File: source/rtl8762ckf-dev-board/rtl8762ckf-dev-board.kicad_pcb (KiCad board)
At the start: 2 copper layers, 87.6 x 17.8 mm, 123 parts, among them J1 u.FL, J2 USB_C_Receptacle_USB2.0, J3 Conn_02x05_Odd_Even, J4 Conn_02x05_Odd_Even, J5 Conn_01x18, J6 boot, J7 Conn_01x03, J9 Conn_01x13, Q1 BC807DS,115, Q2 AO3401A, U2 USBLC6-2SC6, U3 ME6211C33M5G-N, U4 STM32F103C8Tx, U5 RTL8762CKF, Y1 40MHz, Y2 8MHz

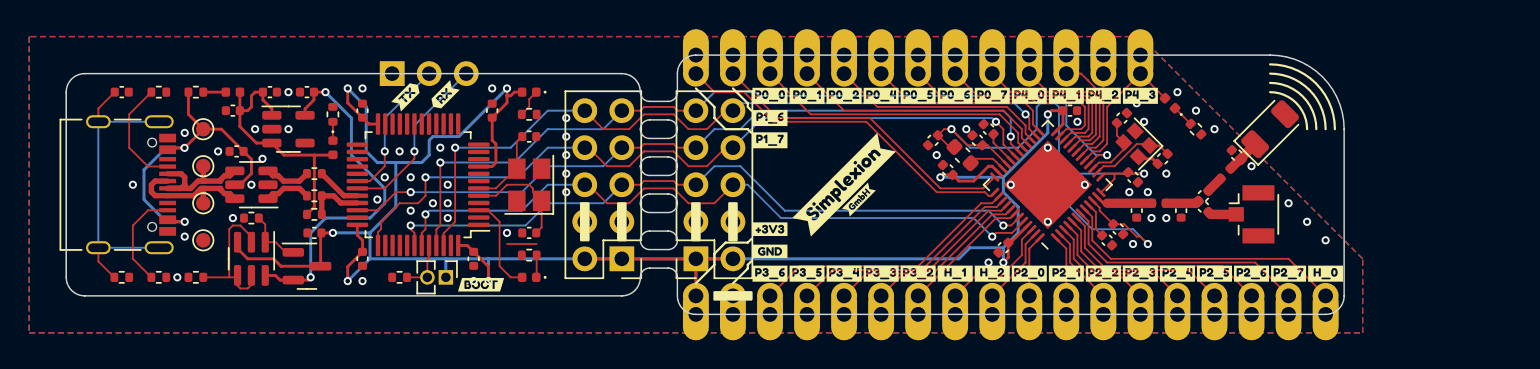
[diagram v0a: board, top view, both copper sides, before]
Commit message: implemented pico probe
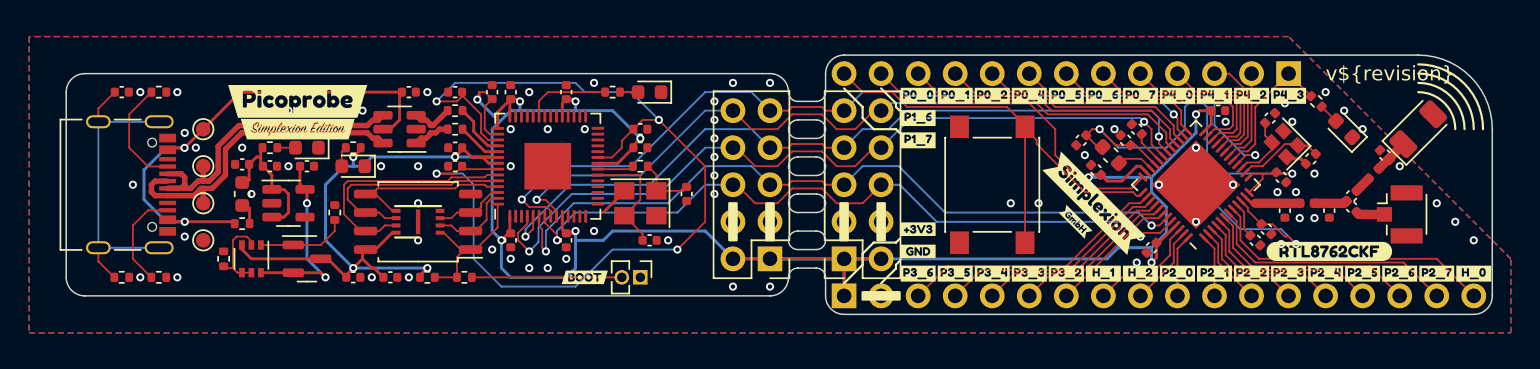
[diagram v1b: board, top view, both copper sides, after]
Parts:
- removed the C22 at (158.8, 130.3)
- removed the J7 at (149.4, 119.4)
- removed J9: Conn_01x13, Connector_Castellated:Castellated_1x13_P2.54mm
- removed the R6 at (149.9, 133.3)
- removed the R7 at (144.0, 127.8)
- removed the R8 at (144.0, 126.2)
- removed the R9 at (144.0, 129.0)
- removed U4: STM32F103C8Tx, Package_QFP:LQFP-48_7x7mm_P0.5mm
- removed kibuzzard-641D9E09: G***, kibuzzard-641D9E09
- removed kibuzzard-641D9E28: G***, kibuzzard-641D9E28
- added C28: 100n, Capacitor_SMD:C_0402_1005Metric, F.Cu at (153.7, 125.7)
- added C29: 100n, Capacitor_SMD:C_0402_1005Metric, F.Cu at (153.7, 124.5)
- added C30: 100n, Capacitor_SMD:C_0402_1005Metric, F.Cu at (161.3, 130.8)
- added C31: 1u, Capacitor_SMD:C_0402_1005Metric, F.Cu at (156.2, 120.7)
- added C32: 100n, Capacitor_SMD:C_0402_1005Metric, F.Cu at (157.5, 130.8)
- added C33: 100n, Capacitor_SMD:C_0402_1005Metric, F.Cu at (157.5, 120.7)
- added C34: 100n, Capacitor_SMD:C_0402_1005Metric, F.Cu at (161.3, 120.7)
- added C35: 100n, Capacitor_SMD:C_0402_1005Metric, F.Cu at (166.4, 124.5)
- added J4: Conn_01x13, Connector_PinHeader_2.54mm:PinHeader_1x13_P2.54mm_Vertical, B.Cu at (210.8, 119.4)
- added NT1: NetTie_2, NetTie_Project:NetTie-2_SMD_Pad0.127mm, F.Cu at (153.7, 121.3)
- added NT2: NetTie_2, NetTie_Project:NetTie-2_SMD_Pad0.127mm, F.Cu at (155.4, 120.7)
- added R10: 1k, Resistor_SMD:R_0402_1005Metric, F.Cu at (154.3, 133.3)
- added R11: 10k, Resistor_SMD:R_0402_1005Metric, F.Cu at (151.8, 133.3)
- added R12: 22, Resistor_SMD:R_0402_1005Metric, F.Cu at (153.7, 123.2)
- added R13: 22, Resistor_SMD:R_0402_1005Metric, F.Cu at (153.7, 121.9)
- added R14: 1k, Resistor_SMD:R_0402_1005Metric, F.Cu at (166.4, 125.7)
- added SW1: SW_Push, Button_Switch_SMD:SW_Push_1P1T_NO_6x6mm_H9.5mm, F.Cu at (190.5, 127.0)
- added U5: W25Q16JV, Package_USON:USON-8_3.0x2.0mm_P0.5mm, F.Cu at (151.1, 129.5)
- added U6: RP2040, Package_DFN_QFN:QFN-56-1EP_7x7mm_P0.4mm_EP3.2x3.2mm, F.Cu at (160.0, 125.7)
- added U7: W25Q128JVS, Package_SO:SOIC-8_5.23x5.23mm_P1.27mm, F.Cu at (151.1, 129.5)
- added kibuzzard-642D5EF2: G***, kibuzzard-642D5EF2, F.Cu at (142.9, 121.3)
- added kibuzzard-642D5F02: G***, kibuzzard-642D5F02, F.Cu at (142.9, 123.2)
- added kibuzzard-642D619C: G***, kibuzzard-642D619C, F.Cu at (213.6, 131.6)
- AE1: value Antenna_Chip -> 2.4GHz
- C12: renamed from C9; value DNP -> C
- C23: value DNP -> 100n
- C24, C25: value 100n -> 33p
- C27: value 100n -> 1u
- C5: renamed from C2; value 3.8p -> 3.9p
- C6: renamed from C3; value DNP -> 22p
- C8: renamed from C5; value 9.2p -> 9.1p
- C9: renamed from C6; value DNP -> C
- D1: renamed from D3; footprint LED_SMD:LED_0402_1005Metric -> LED_SMD:LED_0603_1608Metric
- D2: footprint LED_SMD:LED_0402_1005Metric -> LED_SMD:LED_0603_1608Metric
- D3: renamed from D4; footprint LED_SMD:LED_0402_1005Metric -> LED_SMD:LED_0603_1608Metric
- D4: renamed from D1; footprint LED_SMD:LED_0402_1005Metric -> LED_SMD:LED_0603_1608Metric
- FB1: footprint Inductor_SMD:L_0402_1005Metric -> Inductor_SMD:L_0603_1608Metric
- J5: footprint Connector_Castellated:Castellated_1x18_P2.54mm -> Connector_PinHeader_2.54mm:PinHeader_1x18_P2.54mm_Vertical; moved to B.Cu
- Q1: footprint Package_SO:SC-74-6_1.5x2.9mm_P0.95mm -> Package_TO_SOT_SMD:SOT-363_SC-70-6
- R5: renamed from R1; value 1M -> 10k
- Y2: value 8MHz -> 12M
- moved C25 22.9 mm to (169.5, 127.6)
- moved C24 19.7 mm to (167.0, 130.8), turned to 0 degrees
- moved kibuzzard-641A4D28 17.2 mm to (197.5, 128.3), turned to -45 degrees
- moved D2 15.1 mm to (167.0, 120.7)
- moved kibuzzard-641CD305 14.9 mm to (196.2, 129.5), turned to -45 degrees
- moved C23 13.6 mm to (149.2, 133.3)
- moved J1 13.3 mm to (166.4, 133.3)
- moved D3 13.1 mm to (146.7, 125.7)
- moved R2 12.6 mm to (164.5, 120.7), turned to 180 degrees
- moved C21 12.5 mm to (150.5, 120.7), turned to 180 degrees
- moved R3 12.3 mm to (146.7, 124.5), turned to 0 degrees
- moved D4 12.1 mm to (214.6, 123.2)
- moved C27 11.5 mm to (153.7, 120.7), turned to 180 degrees
- moved U3 10.9 mm to (149.9, 123.2)
- moved C26 10.2 mm to (166.4, 123.2), turned to 0 degrees
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- renumbered C20 to C1, C7 to C10, C8 to C11, C10 to C13, C11 to C14, C12 to C15, C13 to C16, C14 to C17, C15 to C18, C16 to C19, C28 to C2, C17 to C20, C18 to C21, C19 to C22, C21 to C3, C1 to C4, C4 to C7, J6 to J1, J3 to J2, J4 to J3, J1 to J6, J2 to J7, R12 to R1, R11 to R2, R13 to R3, R10 to R4, R2 to R6, R3 to R7, R4 to R8, R5 to R9, U3 to U1, U5 to U2, U2 to U3
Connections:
- net /swlink Black Magic Probe/JTAG.TCK renamed /RP2040/GPIO2
- net /swlink Black Magic Probe/JTAG.TMS renamed /RP2040/GPIO3
- net /swlink Black Magic Probe/USART.DTR renamed /RP2040/GPIO7
- net /swlink Black Magic Probe/USART.RTS renamed /RP2040/GPIO6
- net /swlink Black Magic Probe/USART.RX renamed /RP2040/GPIO5
- net /swlink Black Magic Probe/USART.TX renamed /RP2040/GPIO4
- C23 pad 1: Net-(U4-PD1) -> +3V3
- C24 pad 1: GND -> /RP2040/XIN
- C24 pad 2: +3V3 -> GND
- C25 pad 1: GND -> Net-(C25-Pad1)
- C25 pad 2: +3V3 -> GND
- C26 pad 1: GND -> /RP2040/DVDD
- C26 pad 2: +3V3 -> GND
- C27 pad 1: GND -> /RP2040/VREG_OUT
- C27 pad 2: +3V3 -> GND
- D1 pad 1: Net-(D3-K) -> GND
- D1 pad 2: +5V -> Net-(D1-A)
- D2 pad 1: Net-(D2-K) -> GND
- D2 pad 2: /swlink Black Magic Probe/LED -> Net-(D2-A)
- D3 pad 1: Net-(D4-K) -> GND
- D3 pad 2: +3V3 -> Net-(D3-A)
- D4 pad 1: Net-(D1-K) -> GND
- D4 pad 2: /RTL8762CKF/P4_3 -> Net-(D4-A)
- J1 pad 1: +3V3 -> GND
- J1 pad 2: /swlink Black Magic Probe/BOOT0 -> /RP2040/~{USB_BOOT}
- R1 pad 1: GND -> Net-(D1-A)
- R1 pad 2: Net-(D3-K) -> +5V
- R2 pad 1: GND -> Net-(D2-A)
- R2 pad 2: Net-(D2-K) -> /RP2040/GPIO25
- R3 pad 1: GND -> Net-(D3-A)
- R3 pad 2: Net-(D4-K) -> +3V3
- R4 pad 1: GND -> Net-(D4-A)
- R4 pad 2: Net-(D1-K) -> /RTL8762CKF/P4_3
- U3 pad 1: /Type-C USB 2.0/USB.D+ -> /RP2040/USB.D+
- U3 pad 3: /Type-C USB 2.0/USB.D- -> /RP2040/USB.D-
- Y2 pad 1: Net-(U4-PD0) -> Net-(C25-Pad1)
- Y2 pad 3: Net-(U4-PD1) -> /RP2040/XIN
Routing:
- net /RP2040/DVDD: track 0.00 -> 62.7 mm, vias 0 -> 4
- net +3V3: track 148.4 -> 184.6 mm, vias 8 -> 13
- net /RP2040/QSPI.IO3: track 0.00 -> 17.0 mm
- net /RP2040/QSPI.CLK: track 0.00 -> 15.1 mm
- net /Type-C USB 2.0/D+: track 9.11 -> 21.8 mm
- net /Type-C USB 2.0/D-: track 9.24 -> 22.0 mm
- net VBUS: track 22.7 -> 34.6 mm
- net /RP2040/QSPI.IO0: track 0.00 -> 11.9 mm
- net /swlink Black Magic Probe/USART_{boot}.RX: track 11.7 -> 0.00 mm, vias 1 -> 0
- net /+3V3_{LDO}: track 24.2 -> 12.9 mm
- net /RP2040/QSPI.~{CS}: track 0.00 -> 10.7 mm
- net /RP2040/~{USB_BOOT}: track 0.00 -> 10.3 mm
- net /swlink Black Magic Probe/USART_{boot}.TX: track 9.54 -> 0.00 mm, vias 1 -> 0
- net +5V: track 18.2 -> 9.78 mm
- net /RP2040/XIN: track 0.00 -> 8.35 mm
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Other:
- board size 87.6 x 17.8 mm -> 97.8 x 17.8 mm
- board text added: "JLCJLCJLCJLC"
- board text added: "v${revision}"

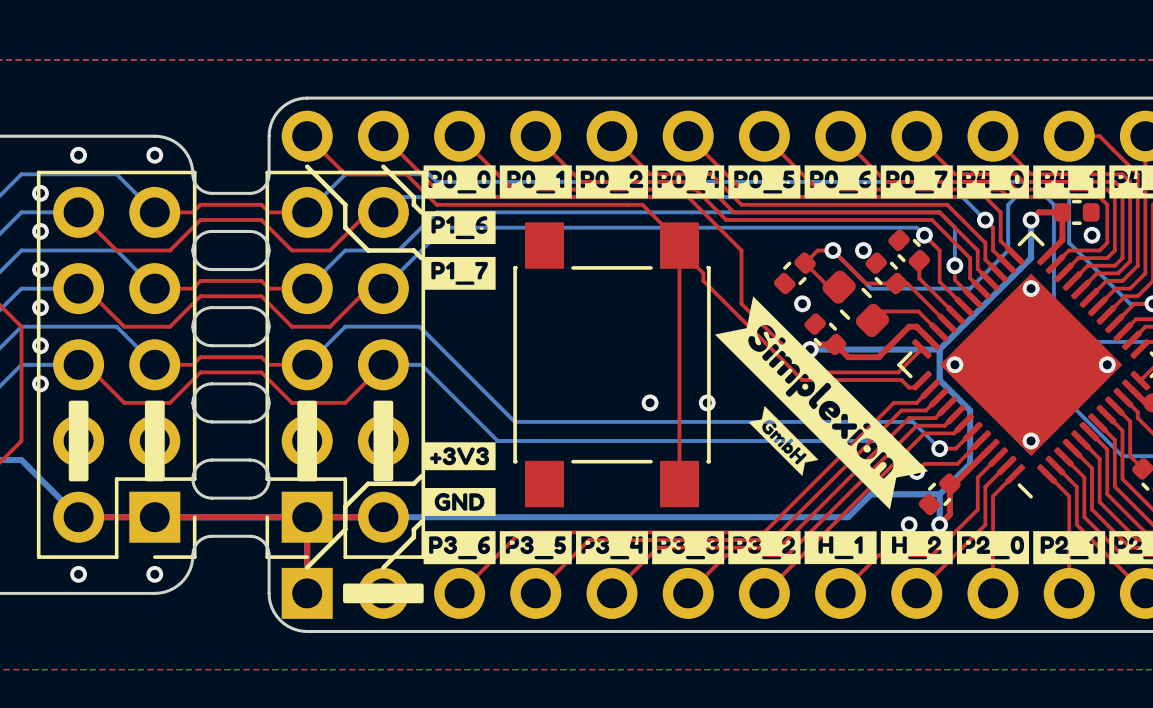
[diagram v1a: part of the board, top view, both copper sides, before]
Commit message: add net ties to uart lines
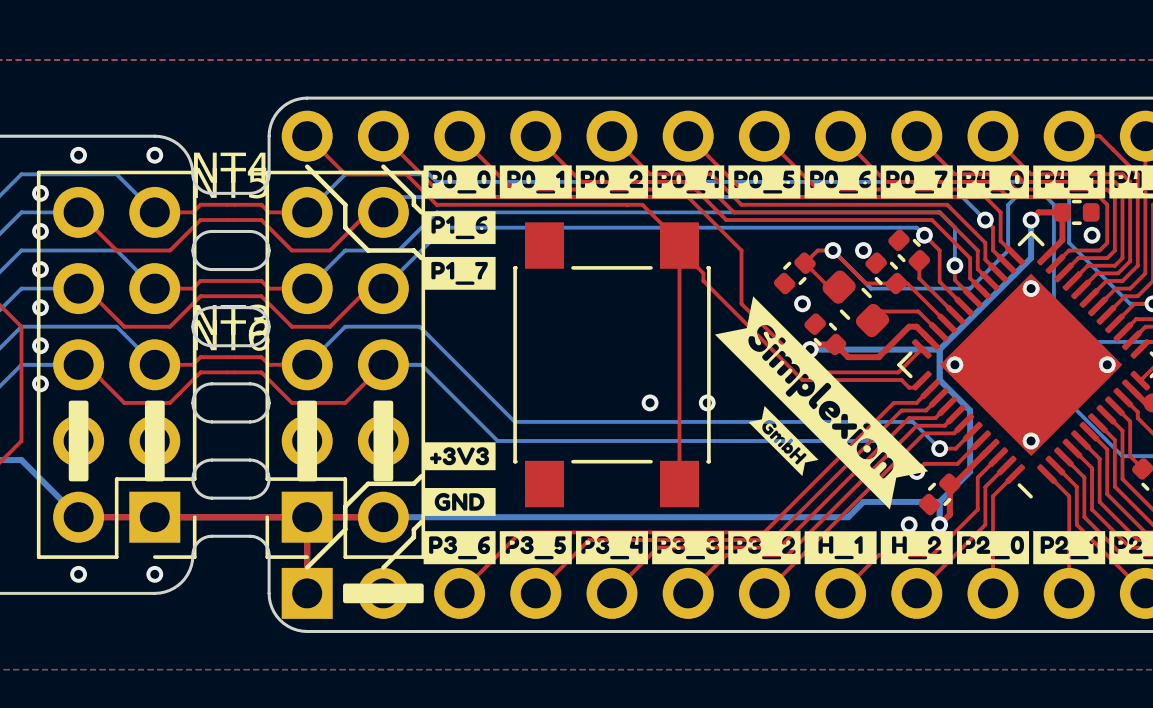
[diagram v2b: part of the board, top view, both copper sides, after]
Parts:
- added NT3: NetTie_2, NetTie_Project:NetTie-2_SMD_Pad0.127mm, F.Cu at (177.8, 126.7)
- added NT4: NetTie_2, NetTie_Project:NetTie-2_SMD_Pad0.127mm, F.Cu at (177.8, 121.7)
- added NT5: NetTie_2, NetTie_Project:NetTie-2_SMD_Pad0.127mm, F.Cu at (177.8, 122.2)
- added NT6: NetTie_2, NetTie_Project:NetTie-2_SMD_Pad0.127mm, F.Cu at (177.8, 127.3)
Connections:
- net /RP2040/GPIO2 renamed /SWD.SWCLK
- net /RP2040/GPIO25 renamed /USB_connected
- net /RP2040/GPIO3 renamed /SWD.SWDIO
- net /RP2040/USB.D+ renamed /USB.D+
- net /RP2040/USB.D- renamed /USB.D-
- net /RTL8762CKF/P1_7 renamed /BUTTON
- net /RTL8762CKF/P4_3 renamed /LED
- J2 pad 10: /RP2040/GPIO7 -> /UART_{RP2040}.DTR
- J2 pad 5: /RP2040/GPIO4 -> /UART_{RP2040}.TX
- J2 pad 6: /RP2040/GPIO5 -> /UART_{RP2040}.RX
- J2 pad 9: /RP2040/GPIO6 -> /UART_{RP2040}.RTS
- J3 pad 10: /RP2040/GPIO7 -> /UART_{RTL8762C}.LOG
- J3 pad 5: /RP2040/GPIO4 -> /UART_{RTL8762C}.RX
- J3 pad 6: /RP2040/GPIO5 -> /UART_{RTL8762C}.TX
- J3 pad 9: /RP2040/GPIO6 -> /UART_{RTL8762C}.RST
- U2 pad 16: /RP2040/GPIO6 -> /UART_{RTL8762C}.RST
- U2 pad 26: /RP2040/GPIO7 -> /UART_{RTL8762C}.LOG
- U2 pad 43: /RP2040/GPIO4 -> /UART_{RTL8762C}.RX
- U2 pad 44: /RP2040/GPIO5 -> /UART_{RTL8762C}.TX
- U6 pad 6: /RP2040/GPIO4 -> /UART_{RP2040}.TX
- U6 pad 7: /RP2040/GPIO5 -> /UART_{RP2040}.RX
- U6 pad 8: /RP2040/GPIO6 -> /UART_{RP2040}.RTS
- U6 pad 9: /RP2040/GPIO7 -> /UART_{RP2040}.DTR
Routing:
- net /RP2040/GPIO6: track 61.5 -> 0.00 mm, vias 2 -> 0
- net /RP2040/GPIO7: track 52.5 -> 0.00 mm, vias 2 -> 0
- net /RP2040/GPIO4: track 51.7 -> 0.00 mm, vias 2 -> 0
- net /RP2040/GPIO5: track 49.9 -> 0.00 mm, vias 2 -> 0
- net /UART_{RTL8762C}.RST: track 0.00 -> 35.5 mm, vias 0 -> 1
- net /UART_{RTL8762C}.LOG: track 0.00 -> 28.3 mm, vias 0 -> 1
- net /UART_{RTL8762C}.TX: track 0.00 -> 27.7 mm, vias 0 -> 1
- net /UART_{RTL8762C}.RX: track 0.00 -> 27.1 mm, vias 0 -> 1
- net /UART_{RP2040}.RTS: track 0.00 -> 25.8 mm, vias 0 -> 1
- net /UART_{RP2040}.TX: track 0.00 -> 24.2 mm, vias 0 -> 1
- net /UART_{RP2040}.DTR: track 0.00 -> 23.9 mm, vias 0 -> 1
- net /UART_{RP2040}.RX: track 0.00 -> 21.9 mm, vias 0 -> 1

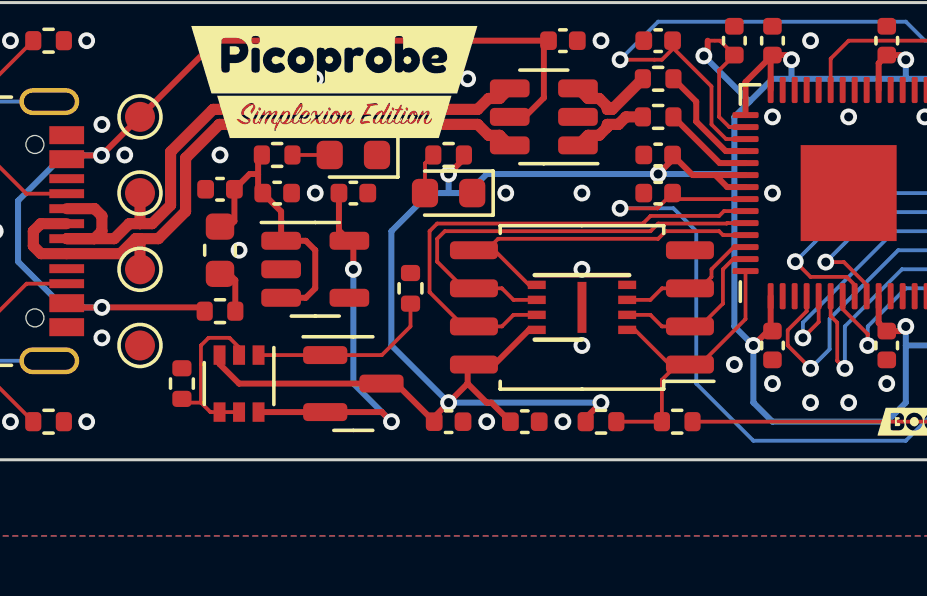
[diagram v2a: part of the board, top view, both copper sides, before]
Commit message: correct zvd; closes #4
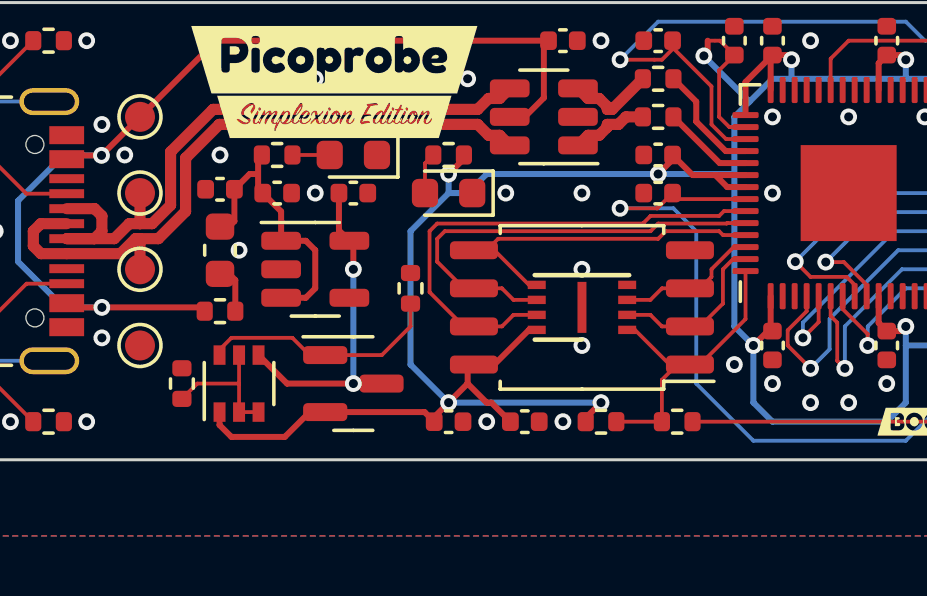
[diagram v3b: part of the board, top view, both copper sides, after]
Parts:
- removed Q1: BC807DS,115, Package_TO_SOT_SMD:SOT-363_SC-70-6
- added Q3: Dual_PNP, Package_TO_SOT_SMD:SOT-363_SC-70-6, F.Cu at (139.7, 132.1)
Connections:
- C2 pad 1: /+3V3_{LDO} -> /ZVD1/A
- Q2 pad 2: /+3V3_{LDO} -> +3V3
- Q2 pad 3: +3V3 -> /ZVD1/A
- U1 pad 5: /+3V3_{LDO} -> /ZVD1/A
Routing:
- net /+3V3_{LDO}: track 12.9 -> 0.00 mm, vias 2 -> 0
- net /ZVD1/A: track 0.00 -> 11.5 mm, vias 0 -> 2
- net Net-(Q2-G): track 6.22 -> 8.10 mm
- net +3V3: track 184.5 -> 183.6 mm
- net Net-(Q3A-B1): track 5.76 -> 4.84 mm
